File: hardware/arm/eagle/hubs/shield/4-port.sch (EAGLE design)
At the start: 11 parts

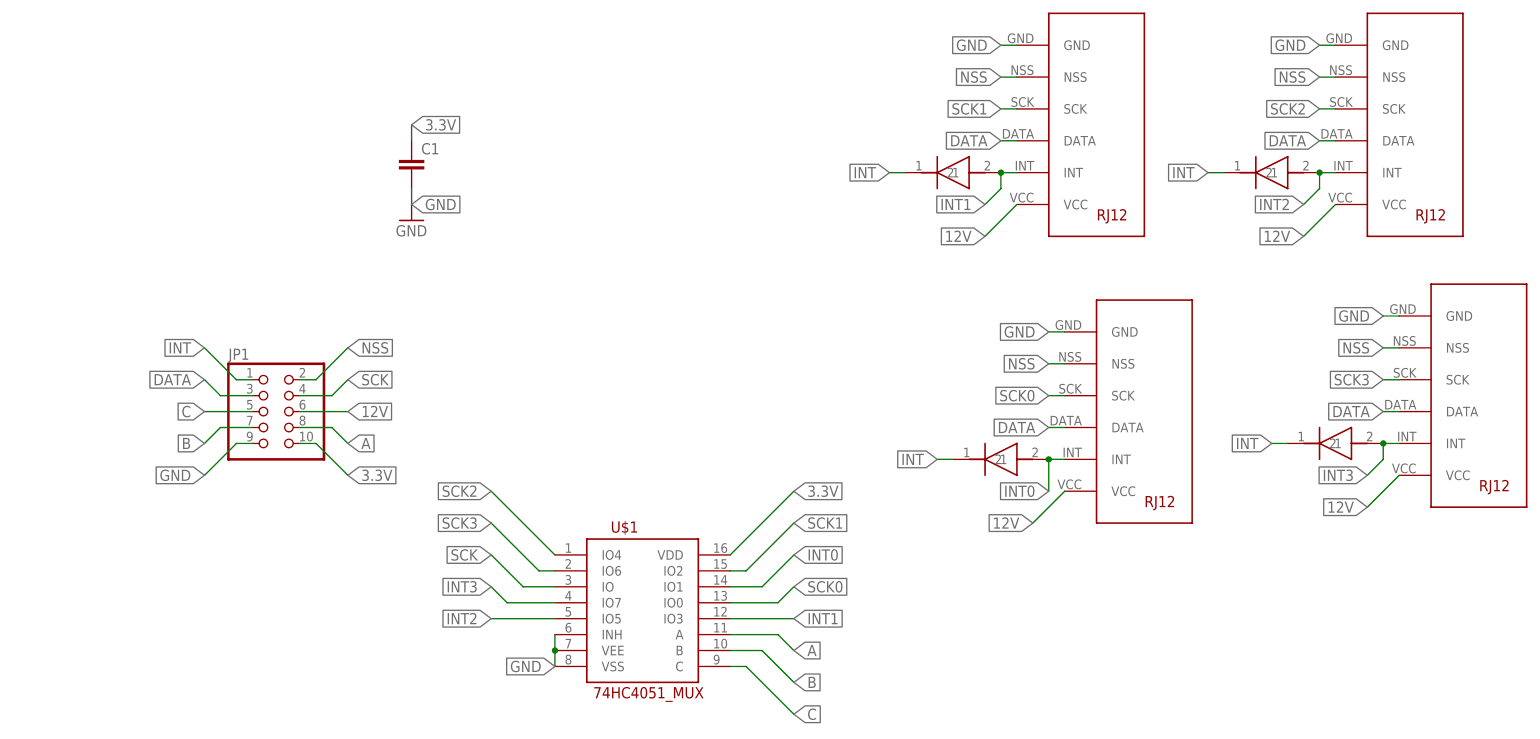
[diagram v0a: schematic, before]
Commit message: 4 port shield pcb
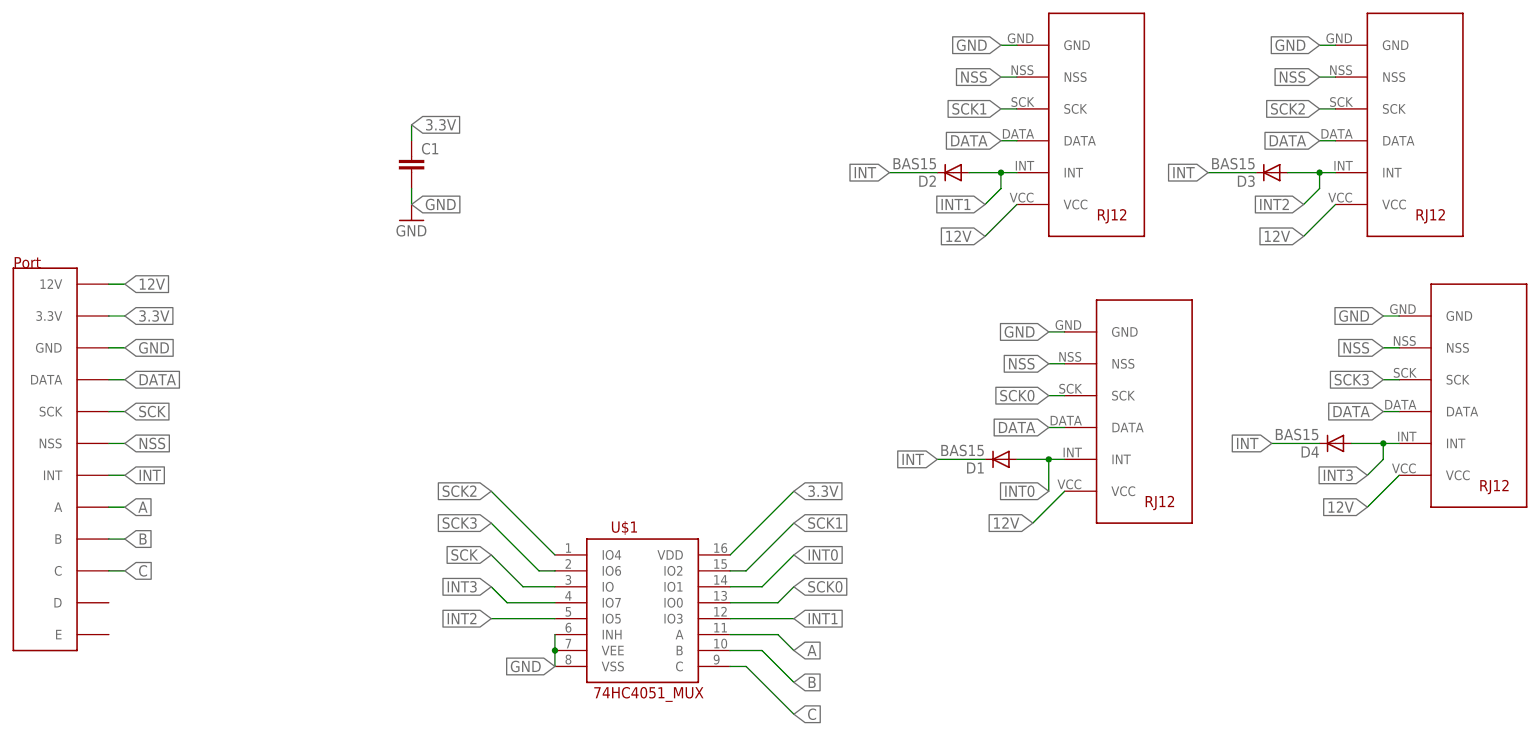
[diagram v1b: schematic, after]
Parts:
- removed JP1: (no value), pinhead:PINHD-2X5
- removed U$6, U$8, U$9: DIODE, gumyns:DIODE
- added D1, D2, D3, D4: BAS15, diode:BAS15
- U$3: value DIODE -> HUB_PORT; device gumyns:DIODE -> gumyns:HUB_PORT
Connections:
- net 12V: now also U$3.12V; no longer JP1.6
- net 3.3V: now also U$3.3.3V; no longer JP1.10
- net A: now also U$3.A; no longer JP1.8
- net B: now also U$3.B; no longer JP1.7
- net C: now also U$3.C; no longer JP1.5
- net DATA: now also U$3.DATA; no longer JP1.3
- net GND: now also U$3.GND; no longer JP1.9
- net INT: now also D1.C, D2.C, D3.C, D4.C, U$3.INT; no longer JP1.1, U$3.1, U$6.1, U$8.1, U$9.1
- net INT0: now also D1.A; no longer U$3.2
- net INT1: now also D2.A; no longer U$9.2
- net INT2: now also D3.A; no longer U$6.2
- net INT3: now also D4.A; no longer U$8.2
- net NSS: now also U$3.NSS; no longer JP1.2
- net SCK: now also U$3.SCK; no longer JP1.4
